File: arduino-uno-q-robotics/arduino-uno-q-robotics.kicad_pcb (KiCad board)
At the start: 2 copper layers, 68.6 x 53.3 mm, 4 parts, among them J1 Conn_02x30_Odd_Even, J2 Conn_02x30_Odd_Even, J3 Connector_FFC-FPC, J4 Connector_FFC-FPC

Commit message: Adjust JMEDIA labels for differential routing
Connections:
- net /CSI0_A0_CLK_M renamed /CSI0_CLK_N
- net /CSI0_A1_LN1_P renamed /CSI0_LN1_P
- net /CSI0_A2_LN2_M renamed /CSI0_LN2_N
- net /CSI0_B0_LN0_P renamed /CSI0_LN0_P
- net /CSI0_B1_LN1_M renamed /CSI0_LN1_N
- net /CSI0_B2_LN3_P renamed /CSI0_LN3_P
- net /CSI0_C0_LN0_M renamed /CSI0_LN0_N
- net /CSI0_C1_LN2_P renamed /CSI0_LN2_P
- net /CSI0_C2_LN3_M renamed /CSI0_LN3_N
- net /CSI0_NC_CLK_P renamed /CSI0_CLK_P
- net /CSI1_A0_CLK_M renamed /CSI1_CLK_N
- net /CSI1_A1_LN1_P renamed /CSI1_LN1_P
- net /CSI1_A2_LN2_M renamed /CSI1_LN2_N
- net /CSI1_B0_LN0_P renamed /CSI1_LN0_P
- net /CSI1_B1_LN1_M renamed /CSI1_LN1_N
- net /CSI1_B2_LN3_P renamed /CSI1_LN3_P
- net /CSI1_C0_LN0_M renamed /CSI1_LN0_N
- net /CSI1_C1_LN2_P renamed /CSI1_LN2_P
- net /CSI1_C2_LN3_M renamed /CSI1_LN3_N
- net /CSI1_NC_CLK_P renamed /CSI1_CLK_P
- net /MIPI_DSI0_CLK_M renamed /MIPI_DSI0_CLK_N
- net /MIPI_DSI0_L0_M renamed /MIPI_DSI0_L0_N
- net /MIPI_DSI0_L1_M renamed /MIPI_DSI0_L1_N
- net /MIPI_DSI0_L2_M renamed /MIPI_DSI0_L2_N
- net /MIPI_DSI0_L3_M renamed /MIPI_DSI0_L3_N
- J3 pad 20: unconnected-(J3-Pad20) -> /SCL_3.3V
- J3 pad 21: unconnected-(J3-Pad21) -> /SDA_3.3V
- J4 pad 20: unconnected-(J4-Pad20) -> /SCL_3.3V
- J4 pad 21: unconnected-(J4-Pad21) -> /SDA_3.3V

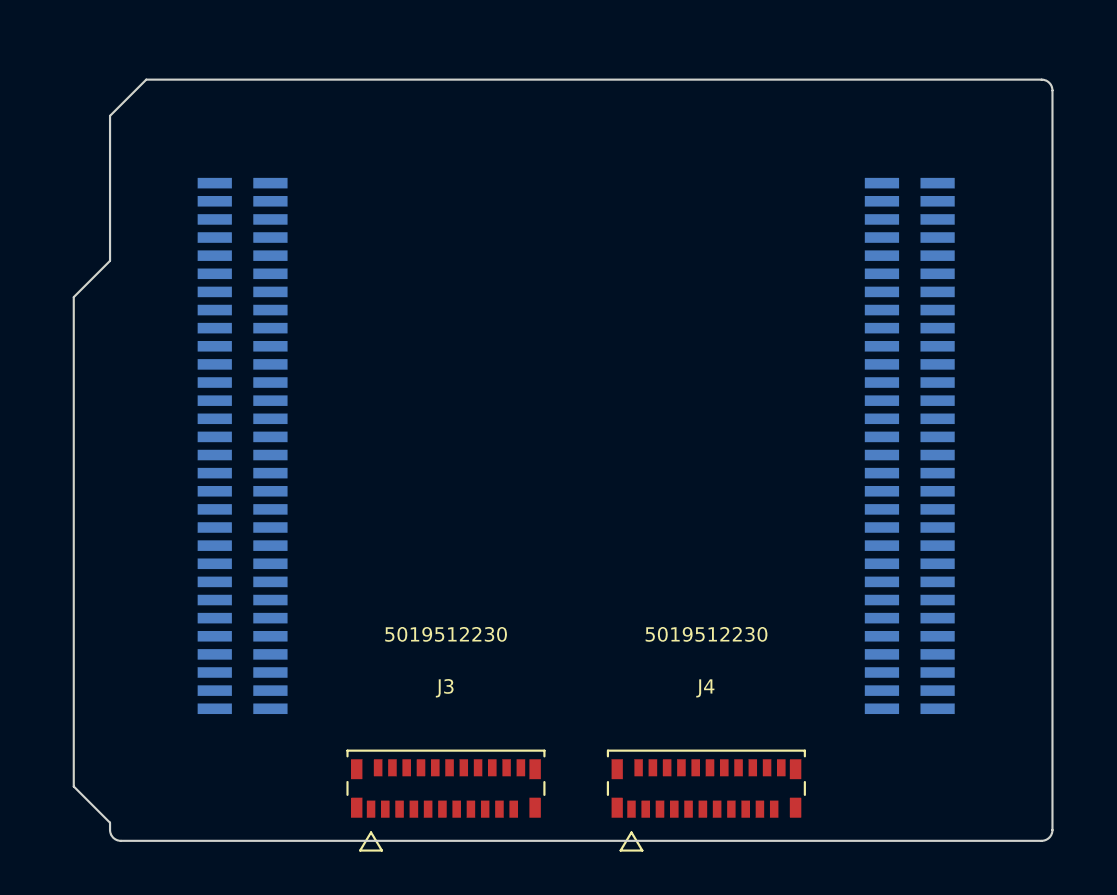
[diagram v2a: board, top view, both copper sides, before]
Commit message: Add GND layers
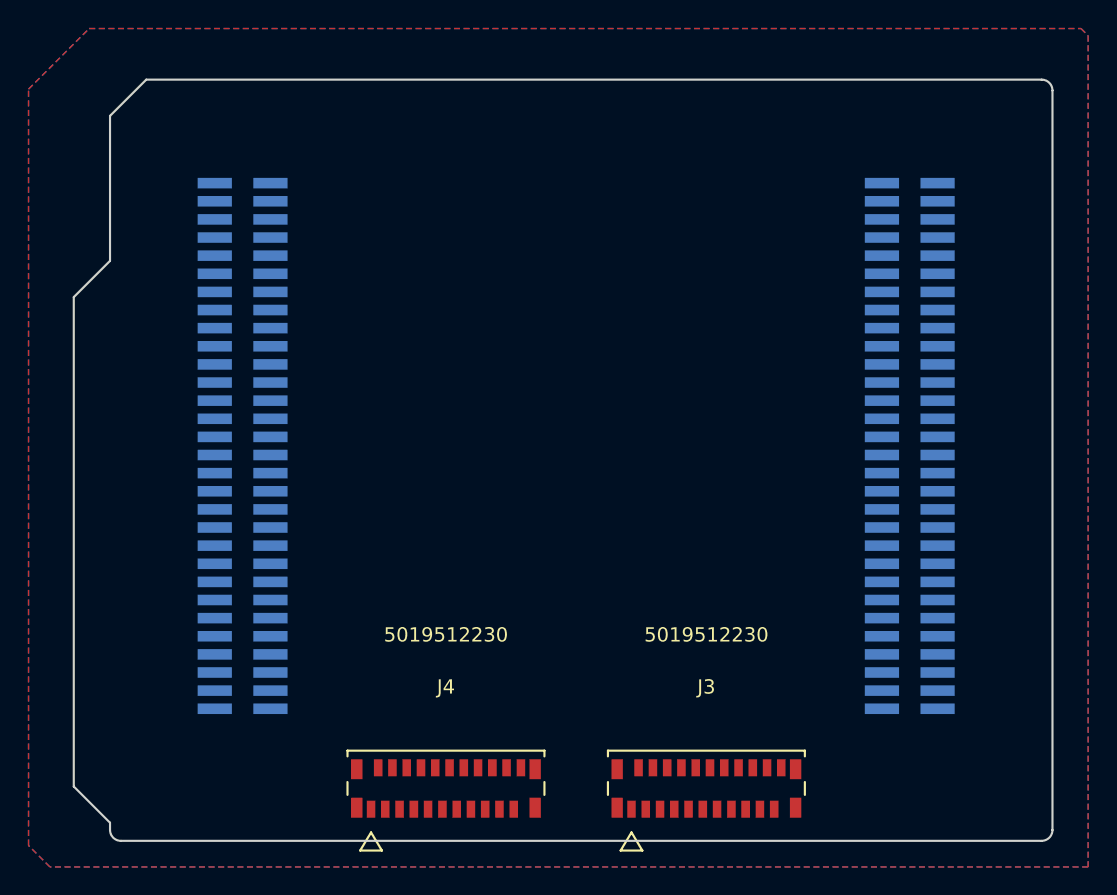
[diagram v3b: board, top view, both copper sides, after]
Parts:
- moved J4 18.3 mm to (140.5, 117.2)
- moved J3 18.2 mm to (158.8, 117.2)
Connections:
- J3 pad 1: unconnected-(J3-Pad1) -> GND
- J3 pad 10: unconnected-(J3-Pad10) -> GND
- J3 pad 11: unconnected-(J3-Pad11) -> /CSI0_LN2_N
- J3 pad 12: unconnected-(J3-Pad12) -> /CSI0_LN2_P
- J3 pad 13: unconnected-(J3-Pad13) -> GND
- J3 pad 14: unconnected-(J3-Pad14) -> /CSI0_LN3_N
- J3 pad 15: unconnected-(J3-Pad15) -> /CSI0_LN3_P
- J3 pad 16: unconnected-(J3-Pad16) -> GND
- J3 pad 19: unconnected-(J3-Pad19) -> GND
- J3 pad 2: unconnected-(J3-Pad2) -> /CSI0_LN0_N
- J3 pad 22: unconnected-(J3-Pad22) -> +3.3V
- J3 pad 3: unconnected-(J3-Pad3) -> /CSI0_LN0_P
- J3 pad 4: unconnected-(J3-Pad4) -> GND
- J3 pad 5: unconnected-(J3-Pad5) -> /CSI0_LN1_N
- J3 pad 6: unconnected-(J3-Pad6) -> /CSI0_LN1_P
- J3 pad 7: unconnected-(J3-Pad7) -> GND
- J3 pad 8: unconnected-(J3-Pad8) -> /CSI0_CLK_N
- J3 pad 9: unconnected-(J3-Pad9) -> /CSI0_CLK_P
- J4 pad 1: unconnected-(J4-Pad1) -> GND
- J4 pad 10: unconnected-(J4-Pad10) -> GND
- J4 pad 11: unconnected-(J4-Pad11) -> /CSI1_LN2_N
- J4 pad 12: unconnected-(J4-Pad12) -> /CSI1_LN2_P
- J4 pad 13: unconnected-(J4-Pad13) -> GND
- J4 pad 14: unconnected-(J4-Pad14) -> /CSI1_LN3_N
- J4 pad 15: unconnected-(J4-Pad15) -> /CSI1_LN3_P
- J4 pad 16: unconnected-(J4-Pad16) -> GND
- J4 pad 19: unconnected-(J4-Pad19) -> GND
- J4 pad 2: unconnected-(J4-Pad2) -> /CSI1_LN0_N
- J4 pad 22: unconnected-(J4-Pad22) -> +3.3V
- J4 pad 3: unconnected-(J4-Pad3) -> /CSI1_LN0_P
- J4 pad 5: unconnected-(J4-Pad5) -> /CSI1_LN1_N
- J4 pad 6: unconnected-(J4-Pad6) -> /CSI1_LN1_P
- J4 pad 7: unconnected-(J4-Pad7) -> GND
- J4 pad 8: unconnected-(J4-Pad8) -> /CSI1_CLK_N
- J4 pad 9: unconnected-(J4-Pad9) -> /CSI1_CLK_P
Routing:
- added copper zone on B.Cu, net GND
- added copper zone on F.Cu, net GND

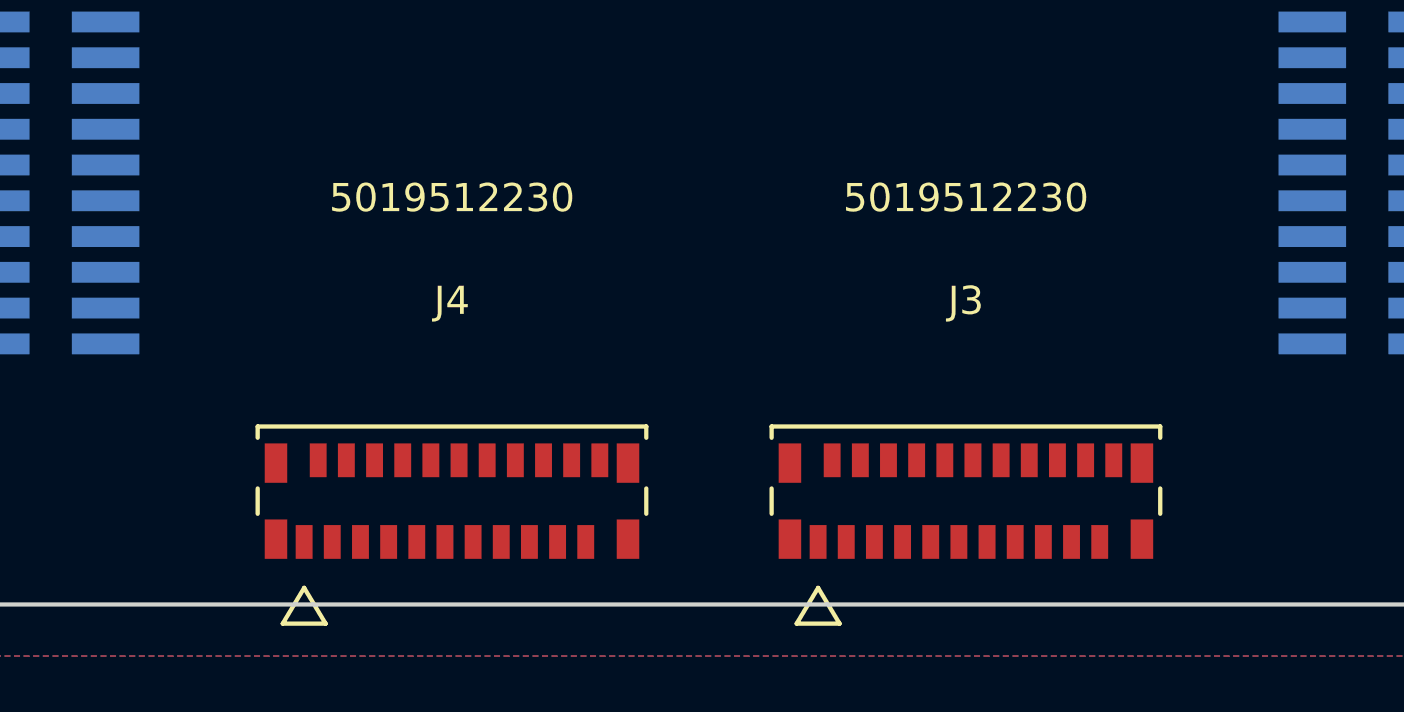
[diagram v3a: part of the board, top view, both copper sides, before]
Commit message: Change FPC footprint and 3D model
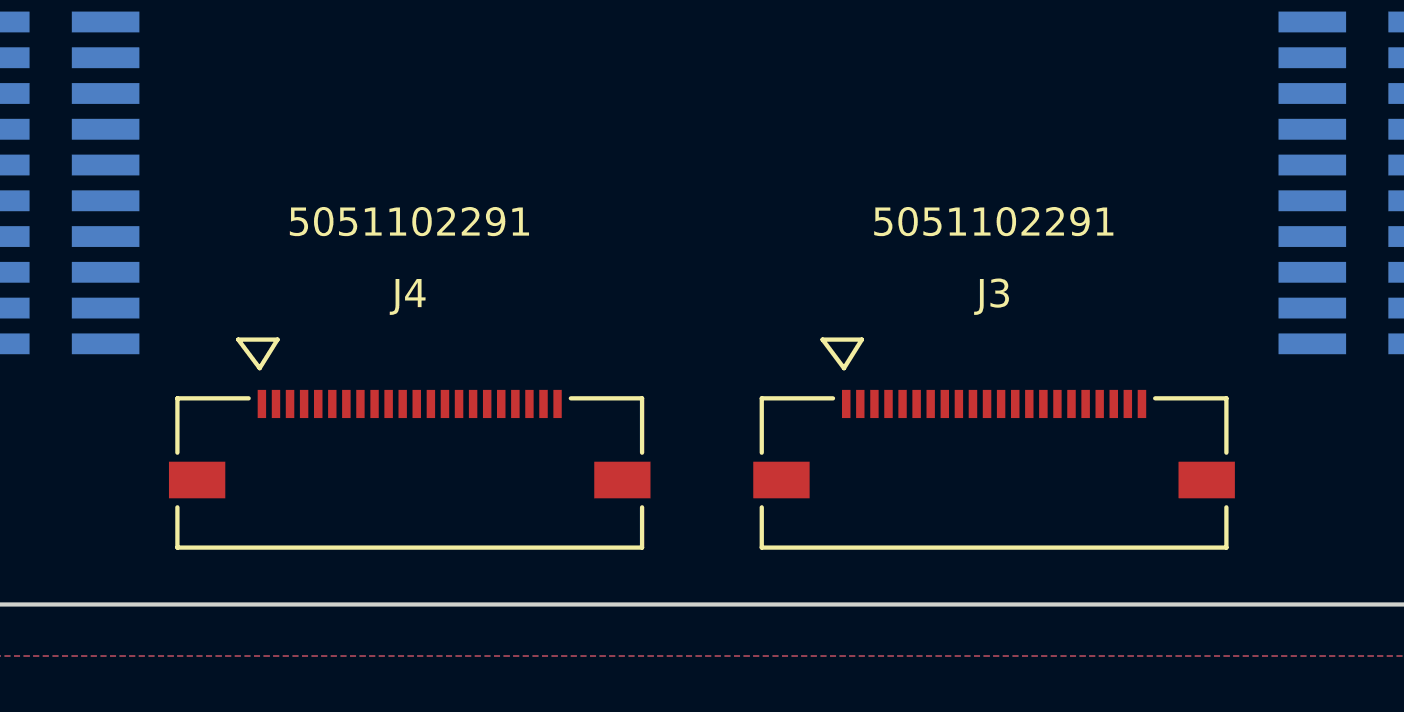
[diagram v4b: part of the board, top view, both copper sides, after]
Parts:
- J3, J4: footprint robotics-footprints:CON_5019512230 -> robotics-footprints:CON_5051102291_MOL
- moved J4 1.80 mm to (139.0, 116.2)
- moved J3 1.41 mm to (159.8, 116.2)

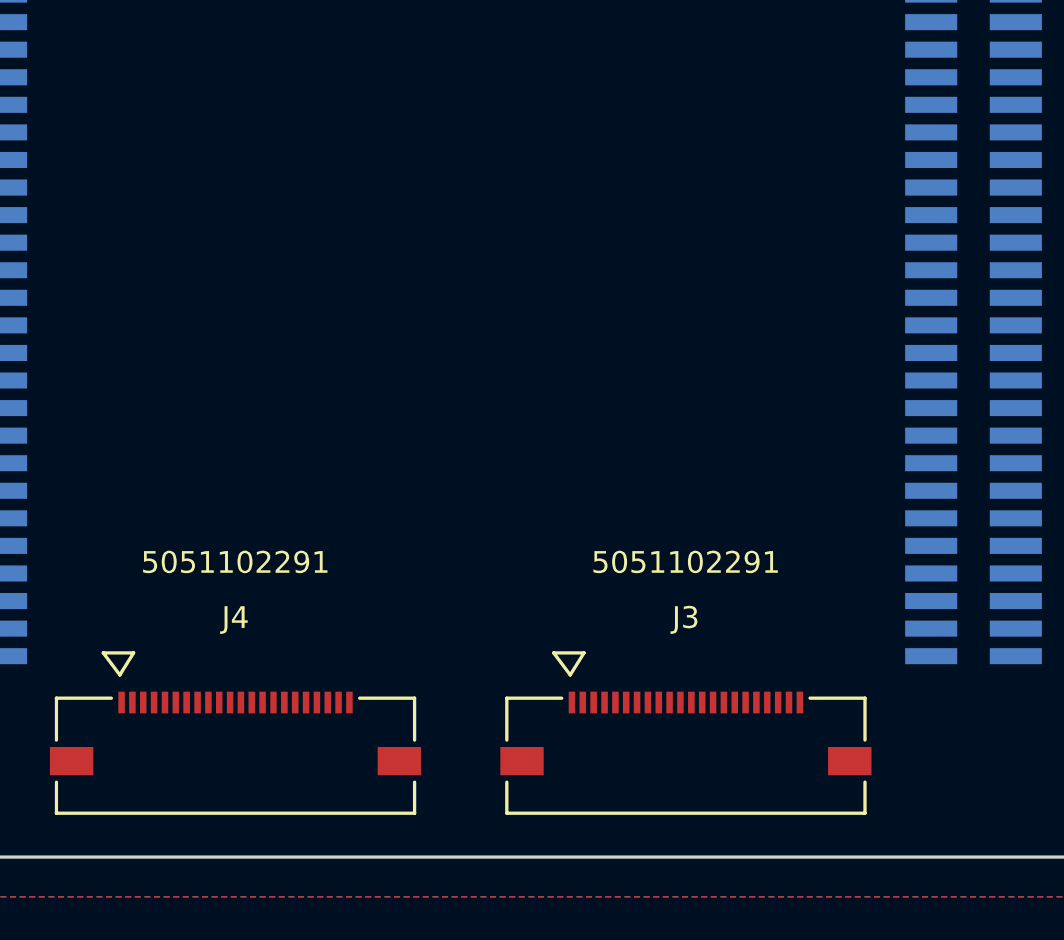
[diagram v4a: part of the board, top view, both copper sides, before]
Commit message: Add PCB constraints
Based on OSHPark 2-layer board

Update constraints
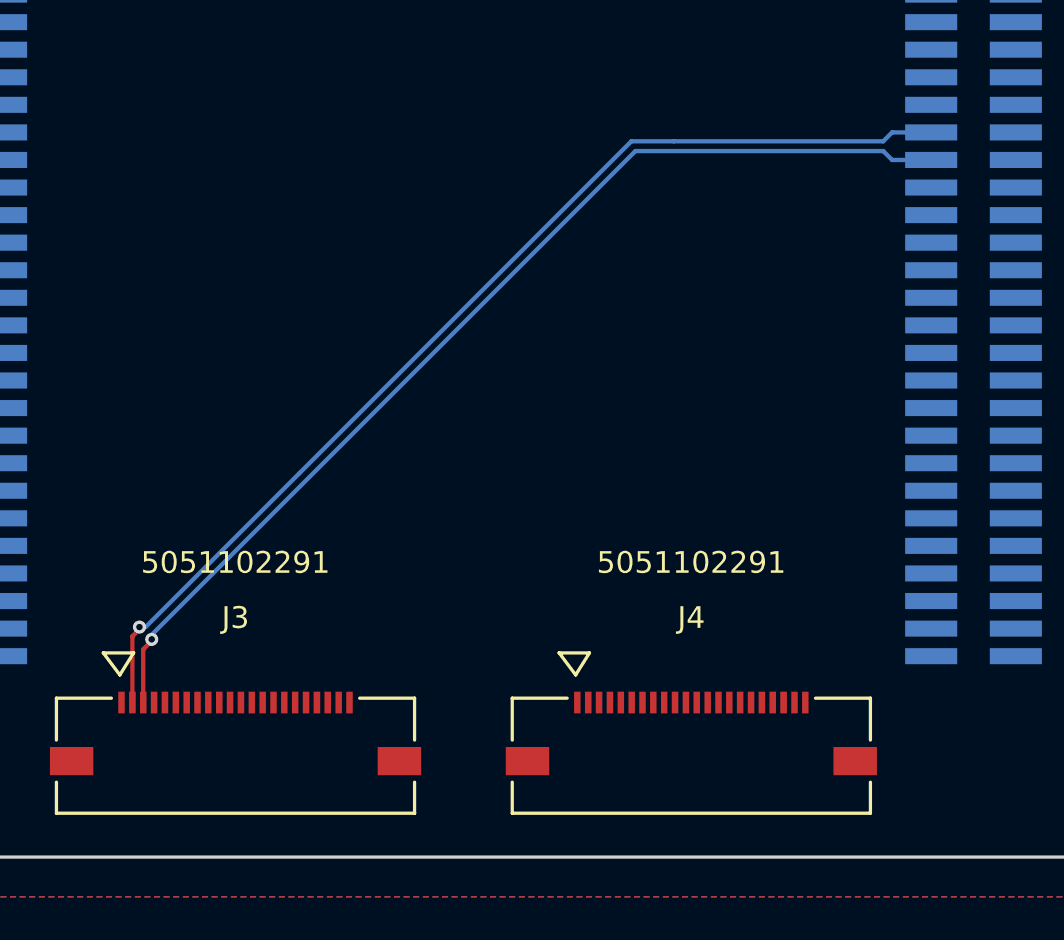
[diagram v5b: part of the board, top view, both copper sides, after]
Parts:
- moved J4 21.0 mm to (160.0, 116.2)
- moved J3 20.8 mm to (139.0, 116.2)
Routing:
- net /CSI0_LN0_N: track 0.00 -> 49.5 mm, vias 0 -> 1
- net /CSI0_LN0_P: track 0.00 -> 48.6 mm, vias 0 -> 1
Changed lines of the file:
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@@
 	)
 	(setup
+		(stackup
+			(layer "F.SilkS"
+				(type "Top Silk Screen")
+			)
+			(layer "F.Paste"
+				(type "Top Solder Paste")
+			)
+			(layer "F.Mask"
+				(type "Top Solder Mask")
+				(thickness 0.01)
+			)
+			(layer "F.Cu"
+				(type "copper")
+				(thickness 0.035)
+			)
+			(layer "dielectric 1"
+				(type "core")
+				(thickness 1.51)
+				(material "FR4")
+				(epsilon_r 4.5)
+				(loss_tangent 0.02)
+			)
+			(layer "B.Cu"
+				(type "copper")
+				(thickness 0.035)
+			)
+			(layer "B.Mask"
+				(type "Bottom Solder Mask")
+				(thickness 0.01)
+			)
+			(layer "B.Paste"
+				(type "Bottom Solder Paste")
+			)
+			(layer "B.SilkS"
+				(type "Bottom Silk Screen")
+			)
+			(copper_finish "None")
+			(dielectric_constraints no)
+		)
 		(pad_to_mask_clearance 0)
 		(allow_soldermask_bridges_in_footprints no)
@@
 	(footprint "robotics-footprints:CON_5051102291_MOL"
 		(layer "F.Cu")
-		(at 139 116.25)
+		(at 160 116.25)
 		(tags "5051102291 ")
 		(property "Reference" "J4"
@@
 	(footprint "robotics-footprints:CON_5051102291_MOL"
 		(layer "F.Cu")
-		(at 159.75 116.25)
+		(at 139 116.25)
 		(tags "5051102291 ")
 		(property "Reference" "J3"
@@
 		(layer "Edge.Cuts")
 	)
+	(segment
+		(start 134.574478 110.324478)
+		(end 134.574478 110.42552)
+		(width 0.2)
+		(layer "F.Cu")
+		(net 87)
+	)
+	(segment
+		(start 134.574478 110.42552)
+		(end 134.249999 110.749999)
+		(width 0.2)
+		(layer "F.Cu")
+		(net 87)
+	)
+	(segment
+		(start 134.249999 110.749999)
+		(end 134.249999 113.8)
+		(width 0.2)
+		(layer "F.Cu")
+		(net 87)
+	)
+	(via
+		(at 134.574478 110.324478)
+		(size 0.6)
+		(drill 0.3)
+		(layers "F.Cu" "B.Cu")
+		(net 87)
+	)
+	(segment
+		(start 157.236801 87.945)
+		(end 159.190834 87.945)
+		(width 0.2)
+		(layer "B.Cu")
+		(net 87)
+	)
+	(segment
+		(start 134.574478 110.324478)
+		(end 134.857323 110.324478)
+		(width 0.2)
+		(layer "B.Cu")
+		(net 87)
+	)
+	(segment
+		(start 134.857323 110.324478)
+		(end 141.951469 103.230332)
+		(width 0.2)
+		(layer "B.Cu")
+		(net 87)
+	)
+	(segment
+		(start 169.249999 87.535)
+		(end 171.05 87.535)
+		(width 0.2)
+		(layer "B.Cu")
+		(net 87)
+	)
+	(segment
+		(start 168.839999 87.945)
+		(end 169.249999 87.535)
+		(width 0.2)
+		(layer "B.Cu")
+		(net 87)
+	)
+	(segment
+		(start 159.190834 87.945)
+		(end 168.839999 87.945)
+		(width 0.2)
+		(layer "B.Cu")
+		(net 87)
+	)
+	(segment
+		(start 141.951469 103.230332)
+		(end 157.236801 87.945)
+		(width 0.2)
+		(layer "B.Cu")
+		(net 87)
+	)
+	(segment
+		(start 135.140165 110.890165)
+		(end 135.140165 110.960877)
+		(width 0.2)
+		(layer "F.Cu")
+		(net 88)
+	)
+	(segment
+		(start 134.75 113.799999)
+		(end 134.750001 113.8)
+		(width 0.2)
+		(layer "F.Cu")
+		(net 88)
+	)
+	(segment
+		(start 134.75 111.351042)
+		(end 134.75 113.799999)
+		(width 0.2)
+		(layer "F.Cu")
+		(net 88)
+	)
+	(segment
+		(start 135.140165 110.960877)
+		(end 134.75 111.351042)
+		(width 0.2)
+		(layer "F.Cu")
+		(net 88)
+	)
+	(via
+		(at 135.140165 110.890165)
+		(size 0.6)
+		(drill 0.3)
+		(layers "F.Cu" "B.Cu")
+		(net 88)
+	)
+	(segment
+		(start 168.839999 88.395)
+		(end 169.249999 88.805)
+		(width 0.2)
+		(layer "B.Cu")
+		(net 88)
+	)
+	(segment
+		(start 135.140165 110.890165)
+		(end 135.140165 110.678034)
+		(width 0.2)
+		(layer "B.Cu")
+		(net 88)
+	)
+	(segment
+		(start 157.423199 88.395)
+		(end 168.839999 88.395)
+		(width 0.2)
+		(layer "B.Cu")
+		(net 88)
+	)
+	(segment
+		(start 169.249999 88.805)
+		(end 171.05 88.805)
+		(width 0.2)
+		(layer "B.Cu")
+		(net 88)
+	)
+	(segment
+		(start 135.140165 110.678034)
+		(end 157.423199 88.395)
+		(width 0.2)
+		(layer "B.Cu")
+		(net 88)
+	)
 	(zone
 		(net 5)
@@
 		(hatch edge 0.5)
 		(connect_pads
-			(clearance 0.5)
+			(clearance 0.4)
 		)
 		(min_thickness 0.25)
@@
 		)
 	)
+	(generated
+		(type tuning_pattern)
+		(name "Tuning Pattern")
+		(layer "B.Cu")
+		(base_line
+			(pts
+				(xy 141.951469 103.230332) (xy 157.236801 87.945) (xy 159.190834 87.945)
+			)
+		)
+		(base_line_coupled
+			(pts
+				(xy 142.269668 103.548531) (xy 142.279185 103.539014)
+			)
+		)
+		(corner_radius_percent 80)
+		(end
+			(xy 159.190834 87.945)
+		)
+		(initial_side "left")
+		(last_diff_pair_gap 0.18)
+		(last_netname "/CSI0_LN0_N")
+		(last_status "too_long")
+		(last_track_width 0.2)
+		(last_tuning "1.3462 mm (too long)")
+		(max_amplitude 1)
+		(min_amplitude 0.2)
+		(min_spacing 0.6)
+		(origin
+			(xy 141.951469 103.230332)
+		)
+		(override_custom_rules no)
+		(rounded yes)
+		(single_sided no)
+		(target_length 1000000)
+		(target_length_max 1000000)
+		(target_length_min 0)
+		(target_skew 0)
+		(target_skew_max 0.1)
+		(target_skew_min -0.1)
+		(tuning_mode "diff_pair_skew")
+		(members "09c48609-23a5-47f1-804c-d8c03bbdc80e" "ebd18ff3-89a4-4da8-9f0c-0952fc0afc23")
+	)
 	(embedded_fonts no)
